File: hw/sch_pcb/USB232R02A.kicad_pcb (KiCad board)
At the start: 2 copper layers, 40.1 x 30 mm, 38 parts, among them J1 USB_B, J10 -, J11 -, J12 -, J13 -, J14 -, J15 -, J16 -, J17 HEADER_2x01_PARALLEL, J2 HEADER_2x03_PARALLEL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

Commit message: Edit
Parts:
- moved R2 10.1 mm to (31.1, -21.5)
- moved R1 10.0 mm to (27.5, -21.5), turned to 0 degrees
- moved JP1 9.38 mm to (29.1, -11.2), turned to -90 degrees
- moved C3 8.13 mm to (21.1, -20.6), turned to 90 degrees
- moved C5 6.71 mm to (30.0, -14.1)
- moved J10 5.08 mm to (25.4, -25.4)
- moved J11 5.08 mm to (27.9, -25.4)
- moved J12 5.08 mm to (22.9, -25.4)
- moved J9 5.08 mm to (30.5, -25.4)
- moved C4 0.54 mm to (23.9, -21.5)
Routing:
- net /TXLED/CBUS2: track 0.00 -> 34.4 mm, vias 0 -> 2
- net +5V: track 0.00 -> 28.7 mm
- net /#RI: track 0.00 -> 22.2 mm, vias 0 -> 1
- net /#DSR: track 0.00 -> 21.8 mm, vias 0 -> 1
- net /RXLED/CBUS1: track 0.00 -> 21.3 mm, vias 0 -> 1
- net /#DCD: track 0.00 -> 20.5 mm, vias 0 -> 1
- net /CBUS0: track 0.00 -> 17.4 mm
- net /CBUS3: track 0.00 -> 15.5 mm, vias 0 -> 2
- net /#DTR: track 0.00 -> 10.8 mm, vias 0 -> 1
- net Net-(R1-Pad2): track 0.00 -> 10.3 mm, vias 0 -> 2
- net /VBUS: track 7.22 -> 16.0 mm
- net Net-(C1-Pad1): track 0.00 -> 5.25 mm
- net +3V3: track 0.00 -> 3.32 mm
- net /RXD: vias 1 -> 0

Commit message: Edit
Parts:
- moved J4 10.2 mm to (30.5, -25.4)
- moved J11 2.54 mm to (25.4, -25.4)
- moved J10 2.54 mm to (22.9, -25.4)
- moved J12 2.54 mm to (20.3, -25.4)
- moved J9 2.54 mm to (27.9, -25.4)
- moved J1 0.25 mm to (15.5, -13.8)
- turned J13 to -90 degrees
- turned J14 to 0 degrees
- turned J16 to 180 degrees
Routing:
- net +5V: track 28.7 -> 69.3 mm, vias 0 -> 3
- net +3V3: track 3.32 -> 26.2 mm, vias 0 -> 3
- net /VCCIO: track 0.00 -> 18.2 mm, vias 0 -> 1
- net GND: track 0.00 -> 14.6 mm, vias 0 -> 16
- net Net-(D2-Pad1): track 0.00 -> 4.05 mm
- net Net-(D3-Pad1): track 0.00 -> 3.51 mm
- net /#DTR: track 10.8 -> 13.8 mm
- net /CBUS0: track 17.4 -> 20.2 mm
- net /TXD: track 8.96 -> 11.5 mm
- net /#RTS: track 8.96 -> 11.5 mm
- net /RXD: track 11.8 -> 14.3 mm, vias 0 -> 1
- net /#CTS: track 15.5 -> 17.7 mm
- net /RXLED/CBUS1: track 21.3 -> 23.3 mm
- net /#RI: track 22.2 -> 23.8 mm
- net /CBUS3: track 15.5 -> 16.4 mm
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- added copper zone on B.Cu, net GND
- added copper zone on F.Cu, net GND

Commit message: Edit
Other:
- board text added: "#CTS"
- board text added: "#DCD"
- board text added: "#DSR"
- board text added: "#DTR"
- board text added: "#RI"
- board text added: "#RTS"
- board text added: "3V3"
- board text added: "5V"
- board text added: "CBUS"
- board text added: "CBUS 1 0 2 3"
- board text added: "GND"
- board text added: "JACHO 2021"
- board text added: "MLAB.CZ USB232R02A"
- board text added: "RX"
- board text added: "TX"
- board text added: "VIO"

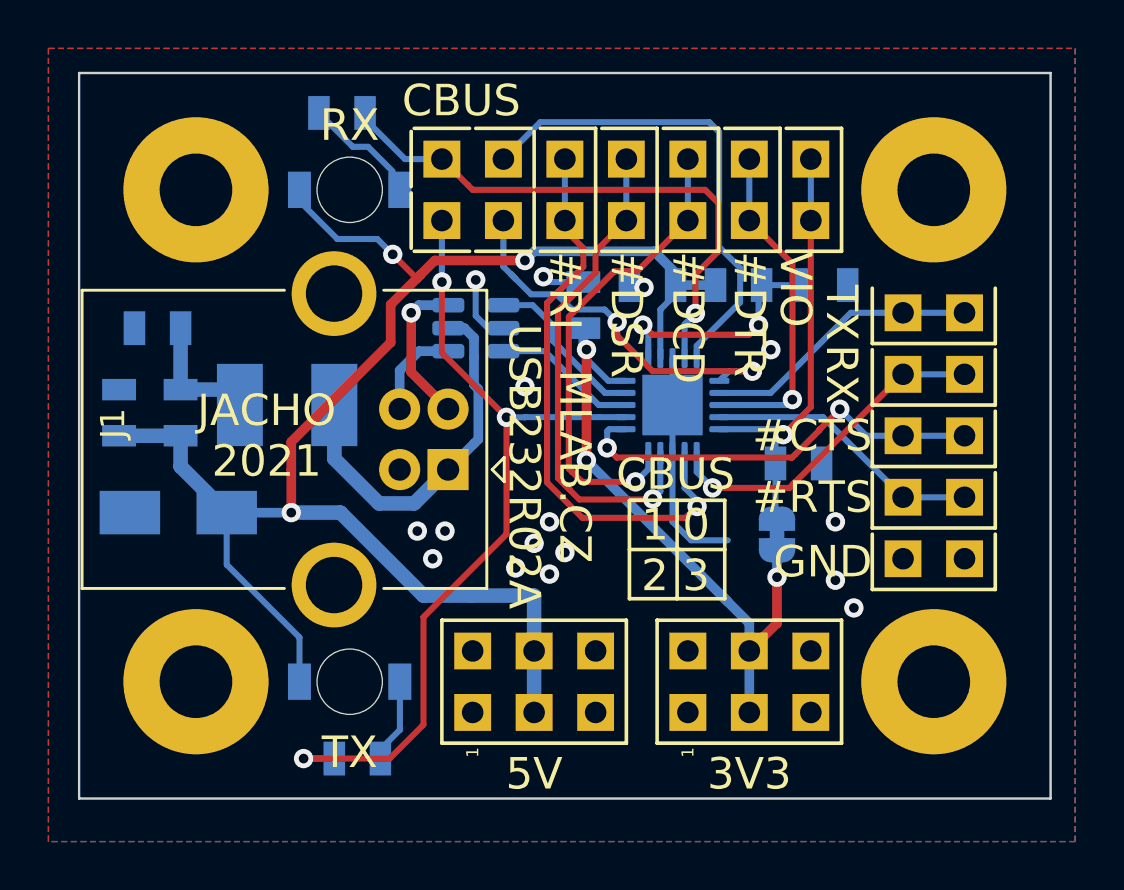
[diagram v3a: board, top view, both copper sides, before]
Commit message: Add MLAB title block. Minor layout cleanup Cleanup silkscreen.
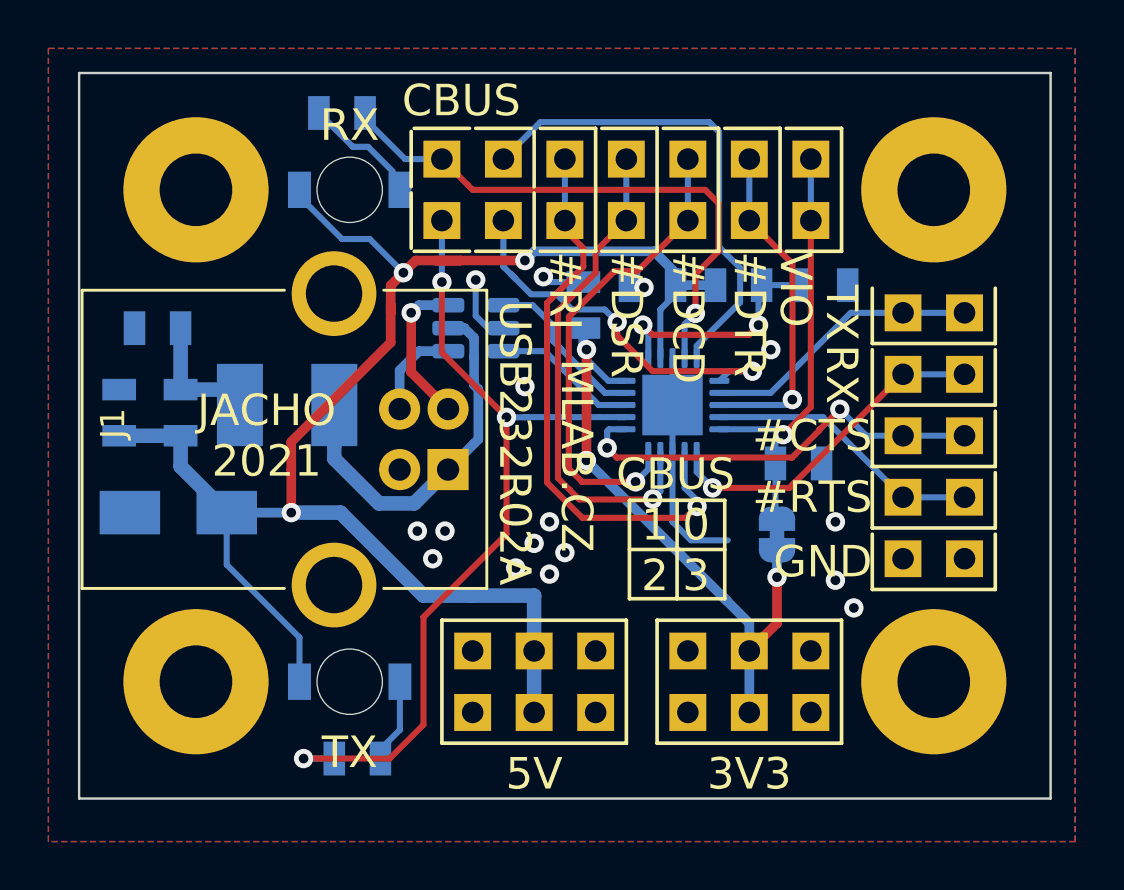
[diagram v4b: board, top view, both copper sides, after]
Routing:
- net +5V: track 69.3 -> 70.2 mm
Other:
- board text added: "MLAB.CZ"
- board text added: "USB232R02A"
- board text removed: "MLAB.CZ USB232R02A"
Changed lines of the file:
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@@
-(kicad_pcb (version 20210126) (generator pcbnew)
+(kicad_pcb (version 20210228) (generator pcbnew)
   (general
     (thickness 1.6)
@@
       (dielectric_constraints no)
     )
+    (pad_to_mask_clearance 0)
     (pcbplotparams
       (layerselection 0x00010fc_ffffffff)
@@
     )
     (fp_line (start -1.6 7.41) (end 2.66 7.41) (layer "F.SilkS") (width 0.12))
-    (fp_line (start -2.32 -0.5) (end -2.32 0.5) (layer "F.SilkS") (width 0.12))
     (fp_line (start -1.6 -4.91) (end -1.6 7.41) (layer "F.SilkS") (width 0.12))
-    (fp_line (start -2.32 0.5) (end -1.82 0) (layer "F.SilkS") (width 0.12))
     (fp_line (start 6.76 -4.91) (end 15.12 -4.91) (layer "F.SilkS") (width 0.12))
     (fp_line (start 2.66 -4.91) (end -1.6 -4.91) (layer "F.SilkS") (width 0.12))
     (fp_line (start 15.12 7.41) (end 6.76 7.41) (layer "F.SilkS") (width 0.12))
-    (fp_line (start -1.82 0) (end -2.32 -0.5) (layer "F.SilkS") (width 0.12))
     (fp_line (start 15.12 -4.91) (end 15.12 7.41) (layer "F.SilkS") (width 0.12))
     (fp_line (start 15.51 9.52) (end 15.51 -7.02) (layer "F.CrtYd") (width 0.05))
@@
       (effects (font (size 1.5 1.5) (thickness 0.15)))
     )
-    (fp_text user "1" (at -2.921 -2.54 90) (layer "F.SilkS")
-      (effects (font (size 0.5 0.5) (thickness 0.05)))
-    )
     (fp_line (start 2.54 3.81) (end -2.54 3.81) (layer "F.SilkS") (width 0.15))
     (fp_line (start -2.54 -3.81) (end 2.54 -3.81) (layer "F.SilkS") (width 0.15))
@@
     (fp_text value "HEADER_2x03_PARALLEL" (at 0 5.08 90) (layer "F.SilkS") hide
       (effects (font (size 1.5 1.5) (thickness 0.15)))
-    )
-    (fp_text user "1" (at -2.921 -2.54 90) (layer "F.SilkS")
-      (effects (font (size 0.5 0.5) (thickness 0.05)))
     )
     (fp_line (start 2.54 3.81) (end -2.54 3.81) (layer "F.SilkS") (width 0.15))
@@
     (effects (font (size 1.3 1.3) (thickness 0.3)) (justify left))
   )
-  (gr_text "MLAB.CZ\nUSB232R02A" (at 19.685 -13.97 270) (layer "F.SilkS")
+  (gr_text "MLAB.CZ" (at 20.8 -14.425 270) (layer "F.SilkS")
     (effects (font (size 1.3 1.3) (thickness 0.3)))
   )
@@
   )
   (gr_text "JACHO\n2021" (at 8.001 -15.24) (layer "F.SilkS")
+    (effects (font (size 1.3 1.3) (thickness 0.3)))
+  )
+  (gr_text "USB232R02A" (at 18.25 -14.95 270) (layer "F.SilkS")
     (effects (font (size 1.3 1.3) (thickness 0.3)))
   )
@@
   (segment (start 10.795 -14.859) (end 10.795 -16.51) (width 0.6) (layer "B.Cu") (net 2))
   (segment (start 16.56751 -18.48449) (end 16.56751 -19.28499) (width 0.4) (layer "B.Cu") (net 2))
-  (segment (start 13.123999 -20.658001) (end 14.203499 -21.737501) (width 0.4) (layer "F.Cu") (net 3))
+  (segment (start 13.123999 -21.448999) (end 13.65 -21.975) (width 0.4) (layer "F.Cu") (net 3))
+  (segment (start 13.123999 -19.092999) (end 13.123999 -20.301001) (width 0.4) (layer "F.Cu") (net 3))
+  (segment (start 13.123999 -20.301001) (end 13.123999 -20.658001) (width 0.4) (layer "F.Cu") (net 3))
   (segment (start 9.017 -13.843) (end 9.017 -14.986) (width 0.4) (layer "F.Cu") (net 3))
-  (segment (start 14.203499 -21.737501) (end 14.351 -21.885002) (width 0.4) (layer "F.Cu") (net 3))
-  (segment (start 14.944998 -22.479) (end 18.669 -22.479) (width 0.4) (layer "F.Cu") (net 3))
-  (segment (start 13.208 -22.733) (end 14.203499 -21.737501) (width 0.25) (layer "F.Cu") (net 3))
+  (segment (start 14.944998 -22.479) (end 16.004 -22.479) (width 0.4) (layer "F.Cu") (net 3))
+  (segment (start 14.154 -22.479) (end 13.65 -21.975) (width 0.4) (layer "F.Cu") (net 3))
+  (segment (start 16.004 -22.479) (end 18.669 -22.479) (width 0.4) (layer "F.Cu") (net 3))
   (segment (start 9.017 -12.065) (end 9.017 -13.843) (width 0.4) (layer "F.Cu") (net 3))
-  (segment (start 14.351 -21.885002) (end 14.944998 -22.479) (width 0.4) (layer "F.Cu") (net 3))
-  (segment (start 13.123999 -19.092999) (end 13.123999 -20.658001) (width 0.4) (layer "F.Cu") (net 3))
+  (segment (start 16.004 -22.479) (end 14.154 -22.479) (width 0.4) (layer "F.Cu") (net 3))
+  (segment (start 13.123999 -20.301001) (end 13.123999 -21.448999) (width 0.4) (layer "F.Cu") (net 3))
   (segment (start 9.017 -14.986) (end 13.123999 -19.092999) (width 0.4) (layer "F.Cu") (net 3))
-  (via (at 13.208 -22.733) (size 0.8) (drill 0.4) (layers "F.Cu" "B.Cu") (net 3))
+  (via (at 13.65 -21.975) (size 0.8) (drill 0.4) (layers "F.Cu" "B.Cu") (net 3))
   (via (at 9.017 -12.065) (size 0.8) (drill 0.4) (layers "F.Cu" "B.Cu") (net 3))
   (via (at 18.669 -22.479) (size 0.8) (drill 0.4) (layers "F.Cu" "B.Cu") (net 3))
   (segment (start 9.017 -12.065) (end 11.049 -12.065) (width 0.6) (layer "B.Cu") (net 3))
-  (segment (start 9.355 -25.4) (end 9.271 -25.4) (width 0.25) (layer "B.Cu") (net 3))
   (segment (start 16.455124 -8.636) (end 19.05 -8.636) (width 0.6) (layer "B.Cu") (net 3))
   (segment (start 1.905 -15.24) (end 4.445 -15.24) (width 0.6) (layer "B.Cu") (net 3))
   (segment (start 24.892 -21.971) (end 24.003 -22.86) (width 0.4) (layer "B.Cu") (net 3))
-  (segment (start 12.573 -23.368) (end 13.208 -22.733) (width 0.25) (layer "B.Cu") (net 3))
   (segment (start 24.003 -22.86) (end 19.05 -22.86) (width 0.4) (layer "B.Cu") (net 3))
-  (segment (start 9.205001 -25.084999) (end 10.922 -23.368) (width 0.25) (layer "B.Cu") (net 3))
   (segment (start 11.049 -12.065) (end 14.478 -8.636) (width 0.6) (layer "B.Cu") (net 3))
+  (segment (start 9.355 -25.125) (end 11.112 -23.368) (width 0.25) (layer "B.Cu") (net 3))
   (segment (start 14.478 -8.636) (end 16.455124 -8.636) (width 0.6) (layer "B.Cu") (net 3))
   (segment (start 19.05 -3.81) (end 19.05 -6.35) (width 0.6) (layer "B.Cu") (net 3))
   (segment (start 24.892 -21.463) (end 24.892 -21.971) (width 0.4) (layer "B.Cu") (net 3))
+  (segment (start 11.112 -23.368) (end 12.257 -23.368) (width 0.25) (layer "B.Cu") (net 3))
   (segment (start 6.35 -12.065) (end 9.017 -12.065) (width 0.4) (layer "B.Cu") (net 3))
-  (segment (start 10.922 -23.368) (end 12.573 -23.368) (width 0.25) (layer "B.Cu") (net 3))
   (segment (start 24.265 -18.4475) (end 24.265 -20.455) (width 0.25) (layer "B.Cu") (net 3))
   (segment (start 4.445 -15.24) (end 4.445 -13.97) (width 0.6) (layer "B.Cu") (net 3))
+  (segment (start 12.257 -23.368) (end 13.65 -21.975) (width 0.25) (layer "B.Cu") (net 3))
   (segment (start 4.445 -13.97) (end 6.35 -12.065) (width 0.6) (layer "B.Cu") (net 3))
   (segment (start 19.05 -22.86) (end 18.669 -22.479) (width 0.4) (layer "B.Cu") (net 3))
@@
   (segment (start 9.355 -5.08) (end 9.355 -6.910002) (width 0.25) (layer "B.Cu") (net 3))
   (segment (start 24.892 -21.082) (end 24.892 -21.463) (width 0.25) (layer "B.Cu") (net 3))
+  (segment (start 9.355 -25.4) (end 9.355 -25.125) (width 0.25) (layer "B.Cu") (net 3))
   (segment (start 19.05 -6.35) (end 19.05 -8.636) (width 0.6) (layer "B.Cu") (net 3))
   (segment (start 26.543 -21.463) (end 24.892 -21.463) (width 0.4) (layer "B.Cu") (net 3))
   (segment (start 9.355 -6.910002) (end 6.35 -9.915002) (width 0.25) (layer "B.Cu") (net 3))
   (segment (start 6.35 -9.915002) (end 6.35 -12.065) (width 0.25) (layer "B.Cu") (net 3))
-  (segment (start 9.271 -25.4) (end 9.205001 -25.334001) (width 0.25) (layer "B.Cu") (net 3))
-  (segment (start 9.205001 -25.334001) (end 9.205001 -25.084999) (width 0.25) (layer "B.Cu") (net 3))
   (segment (start 29.083 -7.493) (end 27.94 -6.35) (width 0.4) (layer "F.Cu") (net 4))
   (segment (start 21.213652 -18.800653) (end 21.213652 -14.228652) (width 0.4) (layer "F.Cu") (net 4))
